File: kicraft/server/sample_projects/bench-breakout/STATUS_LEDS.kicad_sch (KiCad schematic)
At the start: 4 parts

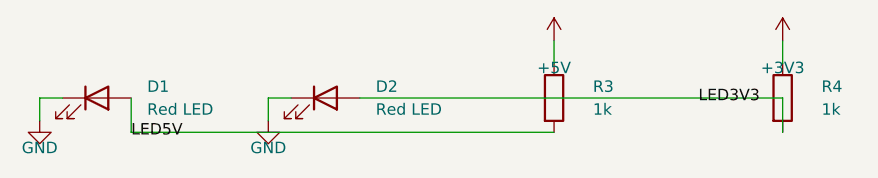
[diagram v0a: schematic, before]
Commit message: feat(showcase): refresh landing samples from self-eval 20260614
Promote the three best boards from self-eval batch 20260614T215540Z
(all grade B) into the landing-page showcase, replacing the regressed
PIR night light (D/45, hit erc_errors + unprogrammable_mcu gates):

- usb-pd-trigger (NEW, featured hero) — 81.0, fab-ready
- weather-sensor (re-promoted; stem A_BMP280_BAROMETRIC -> BMP280_QWIIC_USB_C)
- bench-breakout (re-promoted; 4->5 sheets, 16->19 parts)

Regenerated board.png/hero.png renders and interactive board.glb models
via scripts/promote_to_sample.py. Already live (deploy/restart-web.sh).

Co-Authored-By: Claude Opus 4.8 (1M context) <noreply@anthropic.com>
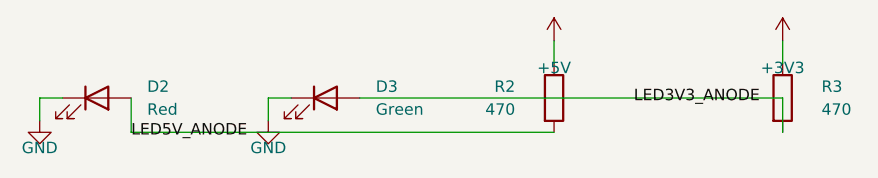
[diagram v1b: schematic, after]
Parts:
- removed D1: Red LED, LED_SMD:LED_0805_2012Metric, symbol Device:LED
- removed R4: 1k, Resistor_SMD:R_0805_2012Metric, symbol Device:R
- added D3: Green, LED_SMD:LED_0805_2012Metric, symbol Device:LED
- added R2: 470, Resistor_SMD:R_0805_2012Metric, symbol Device:R
- D2: value Red LED -> Red
- R3: value 1k -> 470
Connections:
- net +3V3: now also R3.1
- net +5V: now also R2.1; no longer R3.1
- net GND: now also D3.1 (K)
- net LED3V3 renamed LED5V_ANODE
- net LED5V_ANODE: now also R2.2
- net LED5V renamed LED3V3_ANODE
- net LED3V3_ANODE: now also D3.2 (A)
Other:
- moved on the sheet: D2, R3
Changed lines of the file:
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@@
 		(on_board yes)
 		(dnp no)
-		(property "Reference" "D1"
+		(property "Reference" "D2"
 			(at 118.618 105.41 0)
 			(effects (font (size 1.27 1.27)) (justify left))
 		)
-		(property "Value" "Red LED"
+		(property "Value" "Red"
 			(at 118.618 107.95 0)
 			(effects (font (size 1.27 1.27)) (justify left))
@@
 			(effects (font (size 1.27 1.27)) (hide yes))
 		)
-		(property "Description" "5V rail indicator"
+		(property "Description" ""
 			(at 113.03 106.68 0)
 			(effects (font (size 1.27 1.27)) (hide yes))
@@
 		(instances
 			(project "BENCH_BREAKOUT"
-				(path "/3b0eb370-fd3e-44ea-a148-a59507e3cfbd"
-					(reference "D1")
+				(path "/aeb7bb6e-f527-4c40-b22b-a32c069036da"
+					(reference "D2")
 					(unit 1)
 				)
@@
 		(on_board yes)
 		(dnp no)
-		(property "Reference" "D2"
+		(property "Reference" "D3"
 			(at 144.018 105.41 0)
 			(effects (font (size 1.27 1.27)) (justify left))
 		)
-		(property "Value" "Red LED"
+		(property "Value" "Green"
 			(at 144.018 107.95 0)
 			(effects (font (size 1.27 1.27)) (justify left))
@@
 			(effects (font (size 1.27 1.27)) (hide yes))
 		)
-		(property "Description" "3.3V rail indicator"
+		(property "Description" ""
 			(at 138.43 106.68 0)
 			(effects (font (size 1.27 1.27)) (hide yes))
@@
 		(instances
 			(project "BENCH_BREAKOUT"
-				(path "/3b0eb370-fd3e-44ea-a148-a59507e3cfbd"
-					(reference "D2")
+				(path "/aeb7bb6e-f527-4c40-b22b-a32c069036da"
+					(reference "D3")
 					(unit 1)
 				)
@@
 		(on_board yes)
 		(dnp no)
-		(property "Reference" "R3"
-			(at 168.148 105.41 0)
-			(effects (font (size 1.27 1.27)) (justify left))
-		)
-		(property "Value" "1k"
-			(at 168.148 107.95 0)
-			(effects (font (size 1.27 1.27)) (justify left))
+		(property "Reference" "R2"
+			(at 159.512 105.41 0)
+			(effects (font (size 1.27 1.27)) (justify right))
+		)
+		(property "Value" "470"
+			(at 159.512 107.95 0)
+			(effects (font (size 1.27 1.27)) (justify right))
 		)
 		(property "Footprint" "Resistor_SMD:R_0805_2012Metric"
@@
 			(effects (font (size 1.27 1.27)) (hide yes))
 		)
-		(property "Description" "5V LED current limit"
+		(property "Description" ""
 			(at 163.83 106.68 0)
 			(effects (font (size 1.27 1.27)) (hide yes))
@@
 		(instances
 			(project "BENCH_BREAKOUT"
-				(path "/3b0eb370-fd3e-44ea-a148-a59507e3cfbd"
-					(reference "R3")
+				(path "/aeb7bb6e-f527-4c40-b22b-a32c069036da"
+					(reference "R2")
 					(unit 1)
 				)
@@
 		(on_board yes)
 		(dnp no)
-		(property "Reference" "R4"
+		(property "Reference" "R3"
 			(at 193.548 105.41 0)
 			(effects (font (size 1.27 1.27)) (justify left))
 		)
-		(property "Value" "1k"
+		(property "Value" "470"
 			(at 193.548 107.95 0)
 			(effects (font (size 1.27 1.27)) (justify left))
@@
 			(effects (font (size 1.27 1.27)) (hide yes))
 		)
-		(property "Description" "3.3V LED current limit"
+		(property "Description" ""
 			(at 189.23 106.68 0)
 			(effects (font (size 1.27 1.27)) (hide yes))
@@
 		(instances
 			(project "BENCH_BREAKOUT"
-				(path "/3b0eb370-fd3e-44ea-a148-a59507e3cfbd"
-					(reference "R4")
+				(path "/aeb7bb6e-f527-4c40-b22b-a32c069036da"
+					(reference "R3")
 					(unit 1)
 				)
@@
 		(instances
 			(project "BENCH_BREAKOUT"
-				(path "/3b0eb370-fd3e-44ea-a148-a59507e3cfbd"
+				(path "/aeb7bb6e-f527-4c40-b22b-a32c069036da"
 					(reference "#PWR24892")
 					(unit 1)
@@
 		(instances
 			(project "BENCH_BREAKOUT"
-				(path "/3b0eb370-fd3e-44ea-a148-a59507e3cfbd"
+				(path "/aeb7bb6e-f527-4c40-b22b-a32c069036da"
 					(reference "#PWR34107")
 					(unit 1)
@@
 		(instances
 			(project "BENCH_BREAKOUT"
-				(path "/3b0eb370-fd3e-44ea-a148-a59507e3cfbd"
+				(path "/aeb7bb6e-f527-4c40-b22b-a32c069036da"
 					(reference "#PWR08225")
 					(unit 1)
@@
 		(instances
 			(project "BENCH_BREAKOUT"
-				(path "/3b0eb370-fd3e-44ea-a148-a59507e3cfbd"
+				(path "/aeb7bb6e-f527-4c40-b22b-a32c069036da"
 					(reference "#PWR33693")
 					(unit 1)
@@
 		(stroke (width 0) (type default))
 	)
-	(label "LED5V"
+	(label "LED5V_ANODE"
 		(at 116.84 110.49 0)
 		(effects (font (size 1.27 1.27)) (justify left))
 	)
-	(label "LED3V3"
+	(label "LED3V3_ANODE"
 		(at 186.69 106.68 180)
 		(effects (font (size 1.27 1.27)) (justify right))
 	)
 	(sheet_instances
-		(path "/8cde41cc-faa2-4018-99ca-d98eb26713c2"
+		(path "/d7e12d13-11bb-4d62-b32c-ef5309e6501f"
 			(page "STATUS_LEDS")
 		)
